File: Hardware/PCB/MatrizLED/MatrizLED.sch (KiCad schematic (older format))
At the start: 23 parts, among them M1_L1 CONN_01X06, M1_R1 CONN_01X06, M2_L1 CONN_01X06, M2_R1 CONN_01X06, M3_L1 CONN_01X06, M3_R1 CONN_01X06, M4_L1 CONN_01X06, M4_R1 CONN_01X06

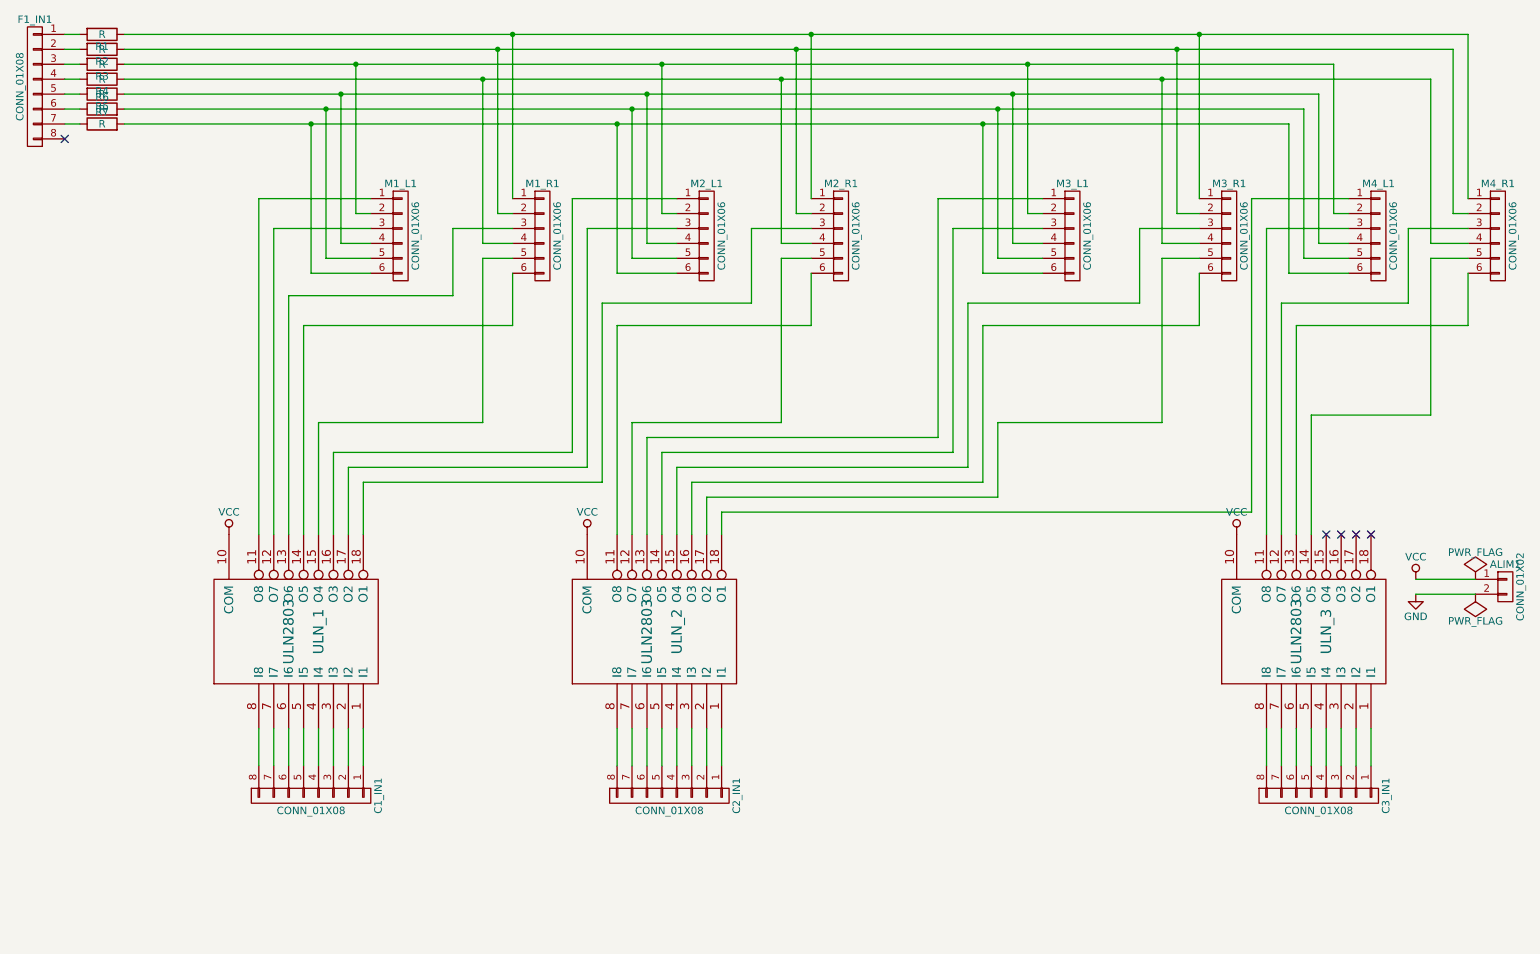
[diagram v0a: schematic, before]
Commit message: Actualizada placa de matrices
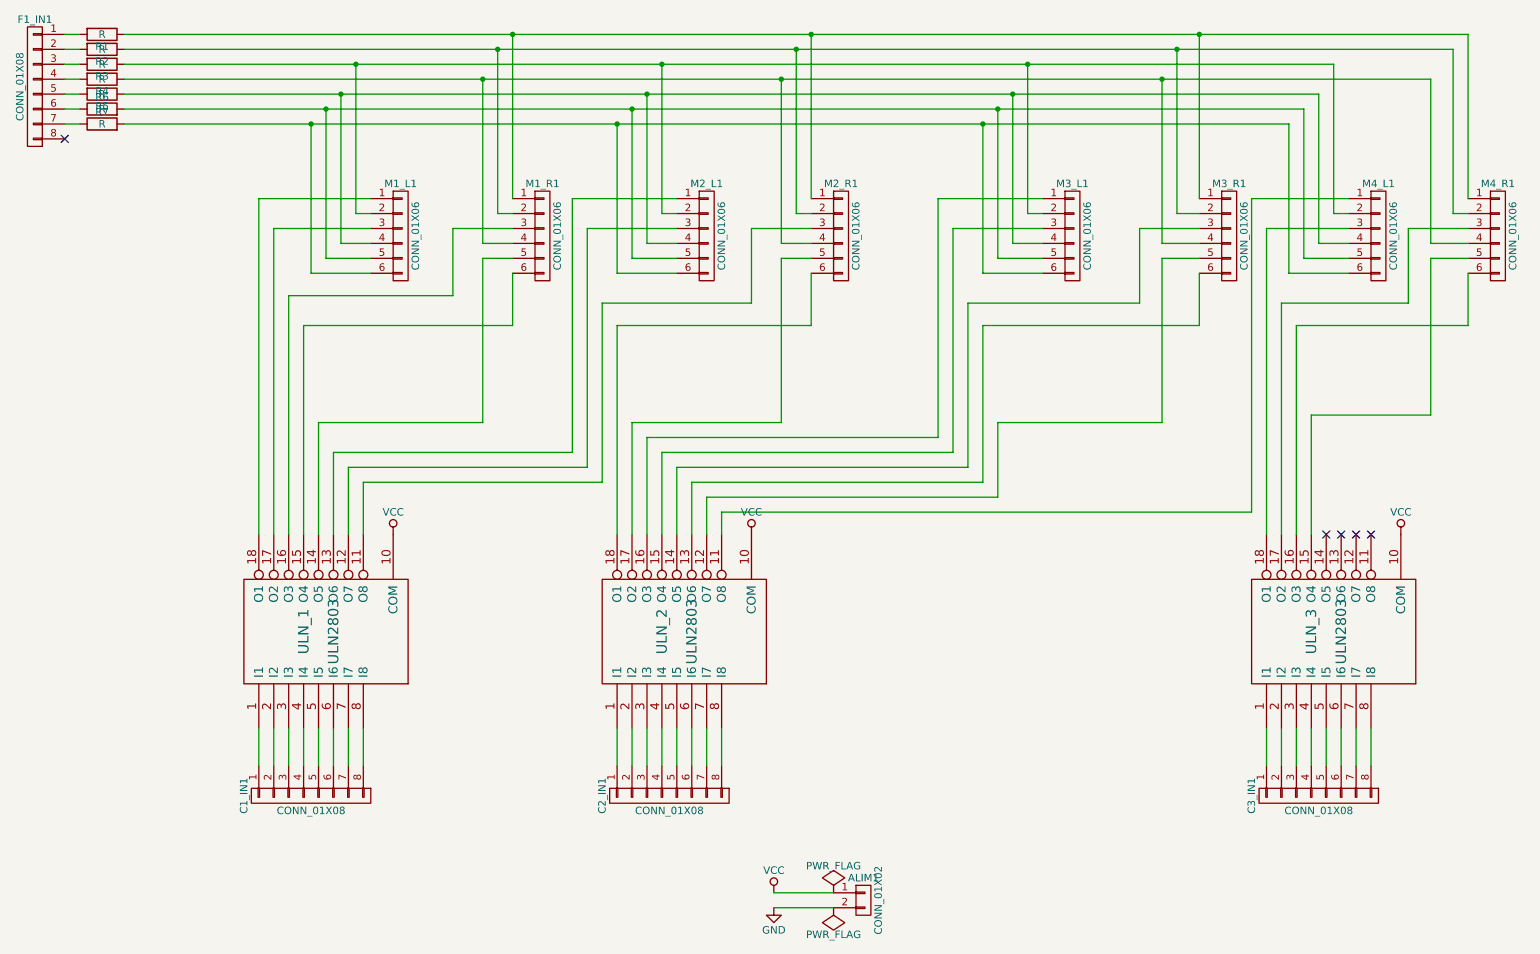
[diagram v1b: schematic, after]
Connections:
- net at M1_L1.1 (P1): now also ULN_1.18 (O1); no longer ULN_1.11 (O8)
- net at M1_L1.3 (P3): now also ULN_1.17 (O2); no longer ULN_1.12 (O7)
- net at M1_R1.3 (P3): now also ULN_1.16 (O3); no longer ULN_1.13 (O6)
- net at M1_R1.5 (P5): now also ULN_1.14 (O5); no longer ULN_1.15 (O4)
- net at M1_R1.6 (P6): now also ULN_1.15 (O4); no longer ULN_1.14 (O5)
- net at M2_L1.1 (P1): now also ULN_1.13 (O6); no longer ULN_1.16 (O3)
- net at M2_L1.3 (P3): now also ULN_1.12 (O7); no longer ULN_1.17 (O2)
- net at M2_R1.3 (P3): now also ULN_1.11 (O8); no longer ULN_1.18 (O1)
- net at M2_R1.5 (P5): now also ULN_2.17 (O2); no longer ULN_2.12 (O7)
- net at M2_R1.6 (P6): now also ULN_2.18 (O1); no longer ULN_2.11 (O8)
- net at M3_L1.1 (P1): now also ULN_2.16 (O3); no longer ULN_2.13 (O6)
- net at M3_L1.3 (P3): now also ULN_2.15 (O4); no longer ULN_2.14 (O5)
- net at M3_R1.3 (P3): now also ULN_2.14 (O5); no longer ULN_2.15 (O4)
- net at M3_R1.5 (P5): now also ULN_2.12 (O7); no longer ULN_2.17 (O2)
- net at M3_R1.6 (P6): now also ULN_2.13 (O6); no longer ULN_2.16 (O3)
- net at M4_L1.1 (P1): now also ULN_2.11 (O8); no longer ULN_2.18 (O1)
- net at M4_L1.3 (P3): now also ULN_3.18 (O1); no longer ULN_3.11 (O8)
- net at M4_R1.3 (P3): now also ULN_3.17 (O2); no longer ULN_3.12 (O7)
- net at M4_R1.5 (P5): now also ULN_3.15 (O4); no longer ULN_3.14 (O5)
- net at M4_R1.6 (P6): now also ULN_3.16 (O3); no longer ULN_3.13 (O6)
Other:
- moved on the sheet: ALIM1, ULN_1, ULN_2, ULN_3
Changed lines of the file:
@@
 F 3 "" H 2850 6300 60  0000 C CNN
 	1    2850 6300
-	0    1    1    0
+	0    -1   1    0
 $EndComp
 $Comp
@@
 F 3 "" H 5250 6300 60  0000 C CNN
 	1    5250 6300
-	0    1    1    0
+	0    -1   1    0
 $EndComp
 $Comp
@@
 F 3 "" H 9600 6300 60  0000 C CNN
 	1    9600 6300
-	0    1    1    0
+	0    -1   1    0
 $EndComp
 $Comp
@@
 L ULN2803 ULN_1
 U 1 1 56A734E8
-P 2800 5200
-F 0 "ULN_1" H 2800 5300 70  0000 C CNN
-F 1 "ULN2803" H 2800 5100 70  0000 C CNN
-F 2 "Housings_DIP:DIP-18_W7.62mm" H 2800 5200 60  0001 C CNN
-F 3 "" H 2800 5200 60  0000 C CNN
-	1    2800 5200
-	0    1    -1   0
+P 2900 5200
+F 0 "ULN_1" H 2900 5300 70  0000 C CNN
+F 1 "ULN2803" H 2900 5100 70  0000 C CNN
+F 2 "Housings_DIP:DIP-18_W7.62mm" H 2900 5200 60  0001 C CNN
+F 3 "" H 2900 5200 60  0000 C CNN
+	1    2900 5200
+	0    -1   -1   0
 $EndComp
 $Comp
 L ULN2803 ULN_2
 U 1 1 56A73740
-P 5200 5200
-F 0 "ULN_2" H 5200 5300 70  0000 C CNN
-F 1 "ULN2803" H 5200 5100 70  0000 C CNN
-F 2 "Housings_DIP:DIP-18_W7.62mm" H 5200 5200 60  0001 C CNN
-F 3 "" H 5200 5200 60  0000 C CNN
-	1    5200 5200
-	0    1    -1   0
+P 5300 5200
+F 0 "ULN_2" H 5300 5300 70  0000 C CNN
+F 1 "ULN2803" H 5300 5100 70  0000 C CNN
+F 2 "Housings_DIP:DIP-18_W7.62mm" H 5300 5200 60  0001 C CNN
+F 3 "" H 5300 5200 60  0000 C CNN
+	1    5300 5200
+	0    -1   -1   0
 $EndComp
 $Comp
 L ULN2803 ULN_3
 U 1 1 56A73A1E
-P 9550 5200
-F 0 "ULN_3" H 9550 5300 70  0000 C CNN
-F 1 "ULN2803" H 9550 5100 70  0000 C CNN
-F 2 "Housings_DIP:DIP-18_W7.62mm" H 9550 5200 60  0001 C CNN
-F 3 "" H 9550 5200 60  0000 C CNN
-	1    9550 5200
-	0    1    -1   0
+P 9650 5200
+F 0 "ULN_3" H 9650 5300 70  0000 C CNN
+F 1 "ULN2803" H 9650 5100 70  0000 C CNN
+F 2 "Housings_DIP:DIP-18_W7.62mm" H 9650 5200 60  0001 C CNN
+F 3 "" H 9650 5200 60  0000 C CNN
+	1    9650 5200
+	0    -1   -1   0
 $EndComp
 NoConn ~ 9650 4550
@@
 	5600 4400 9150 4400
 Wire Wire Line
-	9250 6100 9250 5850
-Wire Wire Line
-	9350 5850 9350 6100
-Wire Wire Line
-	9450 6100 9450 5850
-Wire Wire Line
-	9550 5850 9550 6100
-Wire Wire Line
-	9650 6100 9650 5850
-Wire Wire Line
-	9750 5850 9750 6100
-Wire Wire Line
-	9850 6100 9850 5850
-Wire Wire Line
-	9950 5850 9950 6100
-Wire Wire Line
-	4900 6100 4900 5850
-Wire Wire Line
-	5000 5850 5000 6100
-Wire Wire Line
-	5100 6100 5100 5850
-Wire Wire Line
-	5200 5850 5200 6100
-Wire Wire Line
-	5300 6100 5300 5850
-Wire Wire Line
-	5400 5850 5400 6100
-Wire Wire Line
-	5500 6100 5500 5850
-Wire Wire Line
-	5600 5850 5600 6100
-Wire Wire Line
-	2500 6100 2500 5850
-Wire Wire Line
-	2600 5850 2600 6100
-Wire Wire Line
-	2700 6100 2700 5850
-Wire Wire Line
-	2800 5850 2800 6100
-Wire Wire Line
-	2900 6100 2900 5850
-Wire Wire Line
-	3000 5850 3000 6100
-Wire Wire Line
-	3100 6100 3100 5850
-Wire Wire Line
-	3200 5850 3200 6100
+	9950 6100 9950 5850
+Wire Wire Line
+	9850 5850 9850 6100
+Wire Wire Line
+	9750 6100 9750 5850
+Wire Wire Line
+	9650 5850 9650 6100
+Wire Wire Line
+	9550 6100 9550 5850
+Wire Wire Line
+	9450 5850 9450 6100
+Wire Wire Line
+	9350 6100 9350 5850
+Wire Wire Line
+	9250 5850 9250 6100
+Wire Wire Line
+	5600 6100 5600 5850
+Wire Wire Line
+	5500 5850 5500 6100
+Wire Wire Line
+	5400 6100 5400 5850
+Wire Wire Line
+	5300 5850 5300 6100
+Wire Wire Line
+	5200 6100 5200 5850
+Wire Wire Line
+	5100 5850 5100 6100
+Wire Wire Line
+	5000 6100 5000 5850
+Wire Wire Line
+	4900 5850 4900 6100
+Wire Wire Line
+	3200 6100 3200 5850
+Wire Wire Line
+	3100 5850 3100 6100
+Wire Wire Line
+	3000 6100 3000 5850
+Wire Wire Line
+	2900 5850 2900 6100
+Wire Wire Line
+	2800 6100 2800 5850
+Wire Wire Line
+	2700 5850 2700 6100
+Wire Wire Line
+	2600 6100 2600 5850
+Wire Wire Line
+	2500 5850 2500 6100
 NoConn ~ 9950 4550
 $Comp
 L VCC #PWR01
 U 1 1 56A81571
-P 2300 4550
-F 0 "#PWR01" H 2300 4400 50  0001 C CNN
-F 1 "VCC" H 2300 4700 50  0000 C CNN
-F 2 "" H 2300 4550 60  0000 C CNN
-F 3 "" H 2300 4550 60  0000 C CNN
-	1    2300 4550
+P 3400 4550
+F 0 "#PWR01" H 3400 4400 50  0001 C CNN
+F 1 "VCC" H 3400 4700 50  0000 C CNN
+F 2 "" H 3400 4550 60  0000 C CNN
+F 3 "" H 3400 4550 60  0000 C CNN
+	1    3400 4550
 	1    0    0    -1
 $EndComp
@@
 L VCC #PWR02
 U 1 1 56A819BB
-P 4700 4550
-F 0 "#PWR02" H 4700 4400 50  0001 C CNN
-F 1 "VCC" H 4700 4700 50  0000 C CNN
-F 2 "" H 4700 4550 60  0000 C CNN
-F 3 "" H 4700 4550 60  0000 C CNN
-	1    4700 4550
+P 5800 4550
+F 0 "#PWR02" H 5800 4400 50  0001 C CNN
+F 1 "VCC" H 5800 4700 50  0000 C CNN
+F 2 "" H 5800 4550 60  0000 C CNN
+F 3 "" H 5800 4550 60  0000 C CNN
+	1    5800 4550
 	1    0    0    -1
 $EndComp
@@
 L VCC #PWR03
 U 1 1 56A81EB5
-P 9050 4550
-F 0 "#PWR03" H 9050 4400 50  0001 C CNN
-F 1 "VCC" H 9050 4700 50  0000 C CNN
-F 2 "" H 9050 4550 60  0000 C CNN
-F 3 "" H 9050 4550 60  0000 C CNN
-	1    9050 4550
+P 10150 4550
+F 0 "#PWR03" H 10150 4400 50  0001 C CNN
+F 1 "VCC" H 10150 4700 50  0000 C CNN
+F 2 "" H 10150 4550 60  0000 C CNN
+F 3 "" H 10150 4550 60  0000 C CNN
+	1    10150 4550
 	1    0    0    -1
 $EndComp
@@
 L CONN_01X02 ALIM1
 U 1 1 56A82EF3
-P 10850 4900
-F 0 "ALIM1" H 10850 5050 50  0000 C CNN
-F 1 "CONN_01X02" V 10950 4900 50  0000 C CNN
-F 2 "Pin_Headers:Pin_Header_Straight_1x02" H 10850 4900 60  0001 C CNN
-F 3 "" H 10850 4900 60  0000 C CNN
-	1    10850 4900
+P 6550 7000
+F 0 "ALIM1" H 6550 7150 50  0000 C CNN
+F 1 "CONN_01X02" V 6650 7000 50  0000 C CNN
+F 2 "Pin_Headers:Pin_Header_Straight_1x02" H 6550 7000 60  0001 C CNN
+F 3 "" H 6550 7000 60  0000 C CNN
+	1    6550 7000
 	1    0    0    -1
 $EndComp
@@
 L VCC #PWR04
 U 1 1 56A830E7
-P 10250 4850
-F 0 "#PWR04" H 10250 4700 50  0001 C CNN
-F 1 "VCC" H 10250 5000 50  0000 C CNN
-F 2 "" H 10250 4850 60  0000 C CNN
-F 3 "" H 10250 4850 60  0000 C CNN
-	1    10250 4850
+P 5950 6950
+F 0 "#PWR04" H 5950 6800 50  0001 C CNN
+F 1 "VCC" H 5950 7100 50  0000 C CNN
+F 2 "" H 5950 6950 60  0000 C CNN
+F 3 "" H 5950 6950 60  0000 C CNN
+	1    5950 6950
 	1    0    0    -1
 $EndComp
@@
 L GND #PWR05
 U 1 1 56A83129
-P 10250 4950
-F 0 "#PWR05" H 10250 4700 50  0001 C CNN
-F 1 "GND" H 10250 4800 50  0000 C CNN
-F 2 "" H 10250 4950 60  0000 C CNN
-F 3 "" H 10250 4950 60  0000 C CNN
-	1    10250 4950
-	1    0    0    -1
-$EndComp
-Wire Wire Line
-	10250 4850 10650 4850
-Wire Wire Line
-	10250 4950 10650 4950
+P 5950 7050
+F 0 "#PWR05" H 5950 6800 50  0001 C CNN
+F 1 "GND" H 5950 6900 50  0000 C CNN
+F 2 "" H 5950 7050 60  0000 C CNN
+F 3 "" H 5950 7050 60  0000 C CNN
+	1    5950 7050
+	1    0    0    -1
+$EndComp
+Wire Wire Line
+	5950 6950 6350 6950
+Wire Wire Line
+	5950 7050 6350 7050
 $Comp
 L PWR_FLAG #FLG06
 U 1 1 56A9158E
-P 10650 4850
-F 0 "#FLG06" H 10650 4945 50  0001 C CNN
-F 1 "PWR_FLAG" H 10650 5030 50  0000 C CNN
-F 2 "" H 10650 4850 60  0000 C CNN
-F 3 "" H 10650 4850 60  0000 C CNN
-	1    10650 4850
+P 6350 6950
+F 0 "#FLG06" H 6350 7045 50  0001 C CNN
+F 1 "PWR_FLAG" H 6350 7130 50  0000 C CNN
+F 2 "" H 6350 6950 60  0000 C CNN
+F 3 "" H 6350 6950 60  0000 C CNN
+	1    6350 6950
 	1    0    0    -1
 $EndComp
@@
 L PWR_FLAG #FLG07
 U 1 1 56A91688
-P 10650 4950
-F 0 "#FLG07" H 10650 5045 50  0001 C CNN
-F 1 "PWR_FLAG" H 10650 5130 50  0000 C CNN
-F 2 "" H 10650 4950 60  0000 C CNN
-F 3 "" H 10650 4950 60  0000 C CNN
-	1    10650 4950
+P 6350 7050
+F 0 "#FLG07" H 6350 7145 50  0001 C CNN
+F 1 "PWR_FLAG" H 6350 7230 50  0000 C CNN
+F 2 "" H 6350 7050 60  0000 C CNN
+F 3 "" H 6350 7050 60  0000 C CNN
+	1    6350 7050
 	-1   0    0    1
 $EndComp

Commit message: Agregadas hojas de datos de componentes utilizados
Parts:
- removed ULN_1, ULN_2, ULN_3: ULN2803, Housings_DIP:DIP-18_W7.62mm, symbol ULN2803
- added U? (x3): ULN2803, symbol ULN2803
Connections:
- net GND: now also U?.9 (GND), U?.9 (GND), U?.9 (GND)
- net VCC: now also U?.10 (COM), U?.10 (COM), U?.10 (COM)
- net at C1_IN1.1 (P1): now also U?.1 (I1)
- net at C1_IN1.2 (P2): now also U?.2 (I2)
- net at C1_IN1.3 (P3): now also U?.3 (I3)
- net at C1_IN1.4 (P4): now also U?.4 (I4)
- net at C1_IN1.5 (P5): now also U?.5 (I5)
- net at C1_IN1.6 (P6): now also U?.6 (I6)
- net at C1_IN1.7 (P7): now also U?.7 (I7)
- net at C1_IN1.8 (P8): now also U?.8 (I8)
- net at C2_IN1.1 (P1): now also U?.1 (I1)
- net at C2_IN1.2 (P2): now also U?.2 (I2)
- net at C2_IN1.3 (P3): now also U?.3 (I3)
- net at C2_IN1.4 (P4): now also U?.4 (I4)
- net at C2_IN1.5 (P5): now also U?.5 (I5)
- net at C2_IN1.6 (P6): now also U?.6 (I6)
- net at C2_IN1.7 (P7): now also U?.7 (I7)
- net at C2_IN1.8 (P8): now also U?.8 (I8)
- net at C3_IN1.1 (P1): now also U?.1 (I1)
- net at C3_IN1.2 (P2): now also U?.2 (I2)
- net at C3_IN1.3 (P3): now also U?.3 (I3)
- net at C3_IN1.4 (P4): now also U?.4 (I4)
- net at C3_IN1.5 (P5): now also U?.5 (I5)
- net at C3_IN1.6 (P6): now also U?.6 (I6)
- net at C3_IN1.7 (P7): now also U?.7 (I7)
- net at C3_IN1.8 (P8): now also U?.8 (I8)
- net at M1_L1.1 (P1): now also U?.18 (O1)
- net at M1_L1.3 (P3): now also U?.17 (O2)
- net at M1_R1.3 (P3): now also U?.16 (O3)
- net at M1_R1.5 (P5): now also U?.14 (O5)
- net at M1_R1.6 (P6): now also U?.15 (O4)
- net at M2_L1.1 (P1): now also U?.13 (O6)
- net at M2_L1.3 (P3): now also U?.12 (O7)
- net at M2_R1.3 (P3): now also U?.11 (O8)
- net at M2_R1.5 (P5): now also U?.17 (O2)
- net at M2_R1.6 (P6): now also U?.18 (O1)
- net at M3_L1.1 (P1): now also U?.16 (O3)
- net at M3_L1.3 (P3): now also U?.15 (O4)
- net at M3_R1.3 (P3): now also U?.14 (O5)
- net at M3_R1.5 (P5): now also U?.12 (O7)
- net at M3_R1.6 (P6): now also U?.13 (O6)
- net at M4_L1.1 (P1): now also U?.11 (O8)
- net at M4_L1.3 (P3): now also U?.18 (O1)
- net at M4_R1.3 (P3): now also U?.17 (O2)
- net at M4_R1.5 (P5): now also U?.15 (O4)
- net at M4_R1.6 (P6): now also U?.16 (O3)
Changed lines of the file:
@@
 	1    0    0    -1
-$EndComp
-$Comp
-L ULN2803 ULN_1
-U 1 1 56A734E8
-P 2900 5200
-F 0 "ULN_1" H 2900 5300 70  0000 C CNN
-F 1 "ULN2803" H 2900 5100 70  0000 C CNN
-F 2 "Housings_DIP:DIP-18_W7.62mm" H 2900 5200 60  0001 C CNN
-F 3 "" H 2900 5200 60  0000 C CNN
-	1    2900 5200
-	0    -1   -1   0
-$EndComp
-$Comp
-L ULN2803 ULN_2
-U 1 1 56A73740
-P 5300 5200
-F 0 "ULN_2" H 5300 5300 70  0000 C CNN
-F 1 "ULN2803" H 5300 5100 70  0000 C CNN
-F 2 "Housings_DIP:DIP-18_W7.62mm" H 5300 5200 60  0001 C CNN
-F 3 "" H 5300 5200 60  0000 C CNN
-	1    5300 5200
-	0    -1   -1   0
-$EndComp
-$Comp
-L ULN2803 ULN_3
-U 1 1 56A73A1E
-P 9650 5200
-F 0 "ULN_3" H 9650 5300 70  0000 C CNN
-F 1 "ULN2803" H 9650 5100 70  0000 C CNN
-F 2 "Housings_DIP:DIP-18_W7.62mm" H 9650 5200 60  0001 C CNN
-F 3 "" H 9650 5200 60  0000 C CNN
-	1    9650 5200
-	0    -1   -1   0
 $EndComp
 NoConn ~ 9650 4550
@@
 	-1   0    0    1
 $EndComp
+$Comp
+L ULN2803 U?
+U 1 1 56CA63BB
+P 5300 5200
+F 0 "U?" H 5300 5300 70  0000 C CNN
+F 1 "ULN2803" H 5300 5100 70  0000 C CNN
+F 2 "" H 5300 5200 60  0000 C CNN
+F 3 "" H 5300 5200 60  0000 C CNN
+	1    5300 5200
+	0    -1   -1   0
+$EndComp
+$Comp
+L ULN2803 U?
+U 1 1 56CA646E
+P 9650 5200
+F 0 "U?" H 9650 5300 70  0000 C CNN
+F 1 "ULN2803" H 9650 5100 70  0000 C CNN
+F 2 "" H 9650 5200 60  0000 C CNN
+F 3 "" H 9650 5200 60  0000 C CNN
+	1    9650 5200
+	0    -1   -1   0
+$EndComp
+$Comp
+L ULN2803 U?
+U 1 1 56CA670B
+P 2900 5200
+F 0 "U?" H 2900 5300 70  0000 C CNN
+F 1 "ULN2803" H 2900 5100 70  0000 C CNN
+F 2 "" H 2900 5200 60  0000 C CNN
+F 3 "" H 2900 5200 60  0000 C CNN
+	1    2900 5200
+	0    -1   -1   0
+$EndComp
 $EndSCHEMATC
